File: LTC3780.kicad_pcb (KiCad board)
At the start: 2 copper layers, 120 x 60 mm, 56 parts, among them J1 Screw_Terminal_01x02, J2 Screw_Terminal_01x02, Q2 IPD100N04S402ATMA1, Q3 IPD100N04S402ATMA1, Q4 IPD100N04S402ATMA1, Q5 IPD100N04S402ATMA1, U1 LTC3780EGPBF

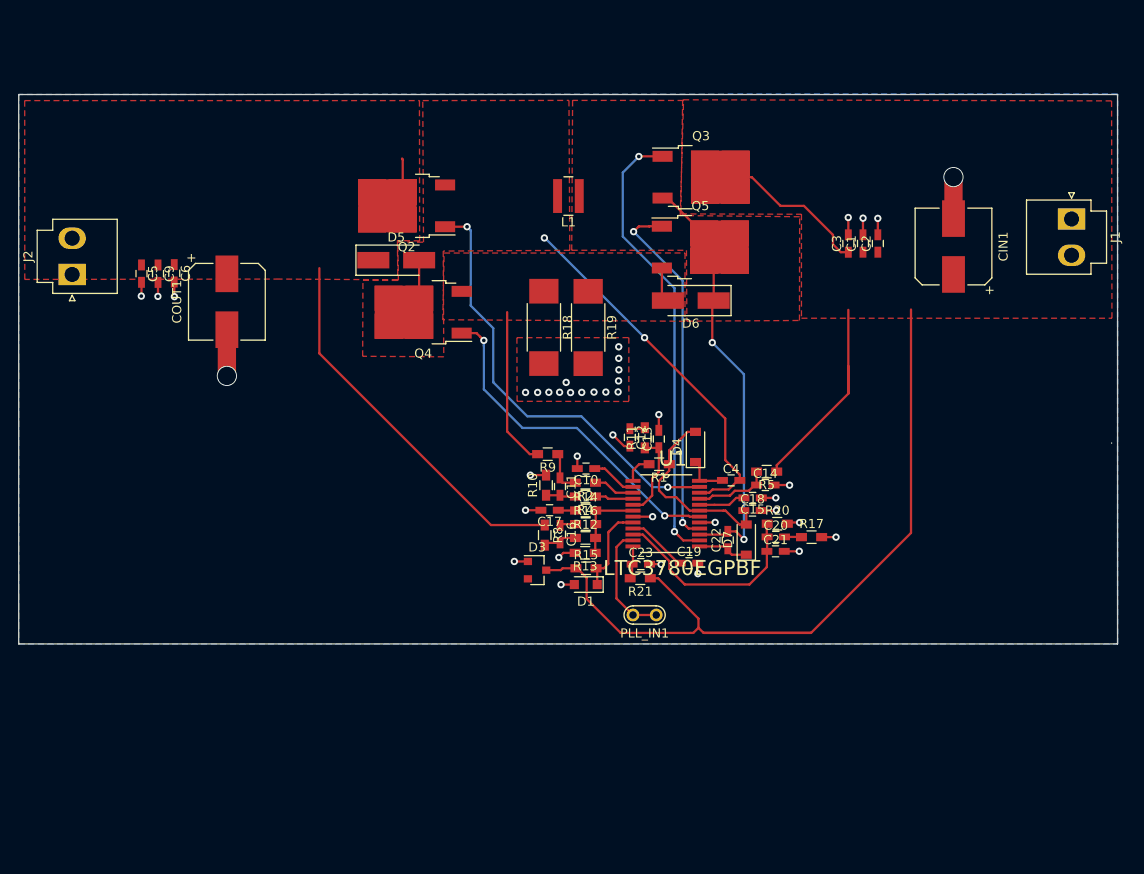
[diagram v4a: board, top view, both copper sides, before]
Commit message: Reduced PCB to 100mm * 60mm and included zip of Gerbers
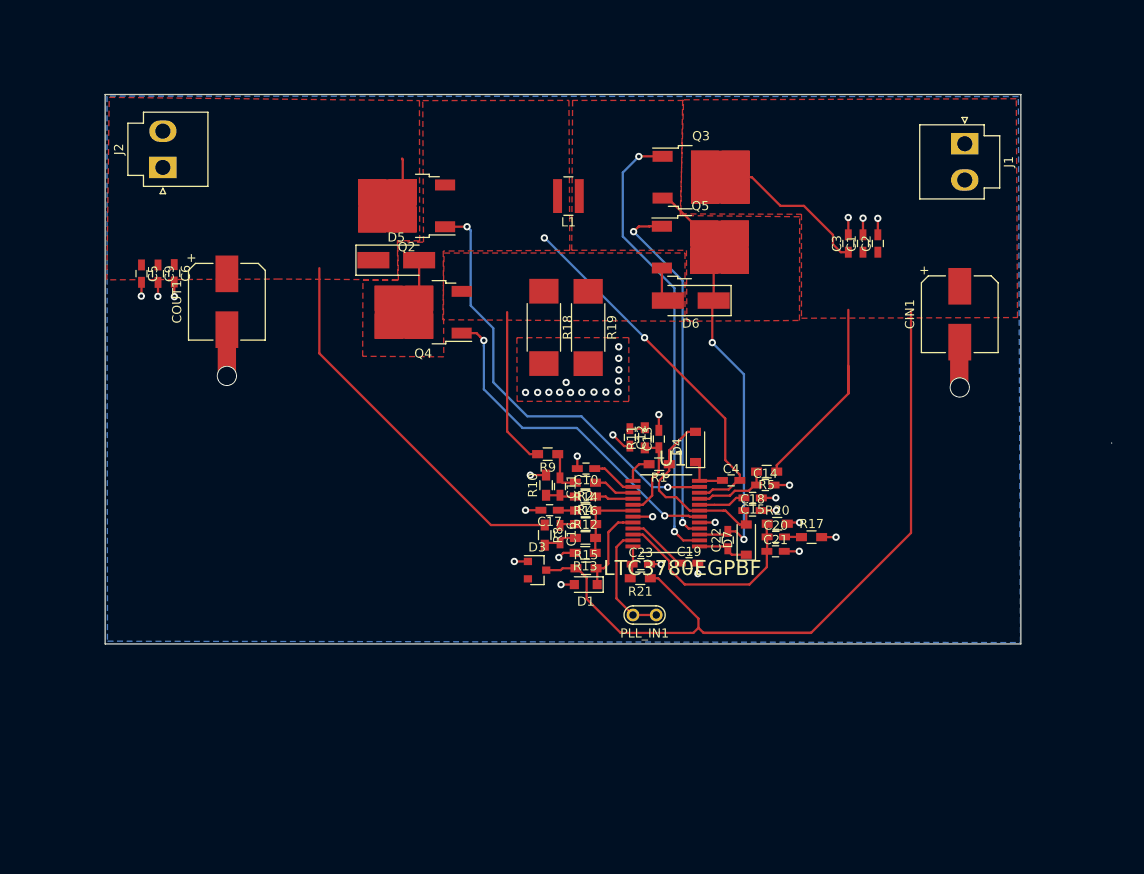
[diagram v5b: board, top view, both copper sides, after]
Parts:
- moved J2 15.3 mm to (124.3, 55.0)
- moved J1 14.3 mm to (211.9, 52.4)
- moved CIN1 7.43 mm to (211.3, 71.0), turned to 270 degrees
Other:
- board size 120 x 60 mm -> 109.9 x 60 mm
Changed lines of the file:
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@@
     (thickness 1.6)
     (drawings 7)
-    (tracks 335)
+    (tracks 334)
     (zones 0)
     (modules 56)
@@
       (outputformat 1)
       (mirror false)
-      (drillshape 1)
+      (drillshape 0)
       (scaleselection 1)
-      (outputdirectory ""))
+      (outputdirectory "/Users/tino/GitHub/LTC3780/gerbers/"))
   )
   (net 0 "")
@@
   )
   (module Connectors_JST:JST_VH_B2P-VH_2x3.96mm_Vertical (layer F.Cu)
-    (at 114.39652 66.66738 90)
+    (at 124.30252 54.9759 90)
     (descr "JST VH series connector, B2P-VH, 3.96mm pitch, top entry type, through hole")
     (tags "connector jst vh vertical")
@@
   )
   (module Connectors_JST:JST_VH_B2P-VH_2x3.96mm_Vertical (layer F.Cu)
-    (at 223.53778 60.60948 270)
+    (at 211.8741 52.39004 270)
     (descr "JST VH series connector, B2P-VH, 3.96mm pitch, top entry type, through hole")
     (tags "connector jst vh vertical")
@@
   )
   (module Capacitors_SMD:CP_Elec_8x6.7 (layer F.Cu)
-    (at 210.6422 63.6143 90)
+    (at 211.328 71.00824 270)
     (descr "SMT capacitor, aluminium electrolytic, 8x6.7")
     (attr smd)
-    (fp_text reference CIN1 (at 0 5.45 90) (layer F.SilkS)
-      (effects (font (size 1 1) (thickness 0.15)))
-    )
-    (fp_text value 22uF (at 0 -5.45 90) (layer F.Fab)
+    (fp_text reference CIN1 (at 0 5.45 270) (layer F.SilkS)
+      (effects (font (size 1 1) (thickness 0.15)))
+    )
+    (fp_text value 22uF (at 0 -5.45 270) (layer F.Fab)
       (effects (font (size 1 1) (thickness 0.15)))
     )
     (fp_circle (center 0 0) (end 1 3.8) (layer F.Fab) (width 0.1))
-    (fp_text user + (at -1.96 -0.08 90) (layer F.Fab)
-      (effects (font (size 1 1) (thickness 0.15)))
-    )
-    (fp_text user + (at -4.78 3.91 90) (layer F.SilkS)
-      (effects (font (size 1 1) (thickness 0.15)))
-    )
-    (fp_text user %R (at 0 5.45 90) (layer F.Fab)
+    (fp_text user + (at -1.96 -0.08 270) (layer F.Fab)
+      (effects (font (size 1 1) (thickness 0.15)))
+    )
+    (fp_text user + (at -4.78 3.91 270) (layer F.SilkS)
+      (effects (font (size 1 1) (thickness 0.15)))
+    )
+    (fp_text user %R (at 0 5.45 270) (layer F.Fab)
       (effects (font (size 1 1) (thickness 0.15)))
     )
@@
     (fp_line (start 5.3 4.29) (end 5.3 -4.29) (layer F.CrtYd) (width 0.05))
     (fp_line (start 5.3 4.29) (end -5.3 4.29) (layer F.CrtYd) (width 0.05))
-    (pad 1 smd rect (at -3.05 0 270) (size 4 2.5) (layers F.Cu F.Paste F.Mask)
+    (pad 1 smd rect (at -3.05 0 90) (size 4 2.5) (layers F.Cu F.Paste F.Mask)
       (net 1 +VSW))
-    (pad 2 smd rect (at 3.05 0 270) (size 4 2.5) (layers F.Cu F.Paste F.Mask)
+    (pad 2 smd rect (at 3.05 0 90) (size 4 2.5) (layers F.Cu F.Paste F.Mask)
       (net 2 GND))
     (model Capacitors_SMD.3dshapes/CP_Elec_8x6.7.wrl
@@
     )
   )
-  (dimension 60.020207 (width 0.15) (layer Dwgs.User)
-    (gr_text "60.00 mm" (at 92 77 90) (layer Dwgs.User)
-      (effects (font (size 1 1) (thickness 0.15)))
-    )
-    (feature1 (pts (xy 108.56468 47.01794) (xy 92.780435 47.010592)))
-    (feature2 (pts (xy 108.53674 107.03814) (xy 92.752495 107.030792)))
-    (crossbar (pts (xy 93.338916 107.031065) (xy 93.366856 47.010865)))
-    (arrow1a (pts (xy 93.366856 47.010865) (xy 93.952752 48.137642)))
-    (arrow1b (pts (xy 93.366856 47.010865) (xy 92.779911 48.137096)))
-    (arrow2a (pts (xy 93.338916 107.031065) (xy 93.925861 105.904834)))
-    (arrow2b (pts (xy 93.338916 107.031065) (xy 92.75302 105.904288)))
-  )
-  (dimension 119.994681 (width 0.15) (layer Dwgs.User)
-    (gr_text "120.00 mm" (at 168.562828 39.37937 360) (layer Dwgs.User)
-      (effects (font (size 1 1) (thickness 0.15)))
-    )
-    (feature1 (pts (xy 228.55936 47.01286) (xy 228.560092 40.099299)))
-    (feature2 (pts (xy 108.56468 47.00016) (xy 108.565412 40.086599)))
-    (crossbar (pts (xy 108.56535 40.67302) (xy 228.56003 40.68572)))
-    (arrow1a (pts (xy 228.56003 40.68572) (xy 227.433464 41.272022)))
-    (arrow1b (pts (xy 228.56003 40.68572) (xy 227.433588 40.09918)))
-    (arrow2a (pts (xy 108.56535 40.67302) (xy 109.691792 41.25956)))
-    (arrow2b (pts (xy 108.56535 40.67302) (xy 109.691916 40.086718)))
+  (dimension 99.979481 (width 0.15) (layer Dwgs.User)
+    (gr_text "100.00 mm" (at 167.995014 42.41734) (layer Dwgs.User)
+      (effects (font (size 1 1) (thickness 0.15)))
+    )
+    (feature1 (pts (xy 118.00586 47.03572) (xy 118.005365 43.137269)))
+    (feature2 (pts (xy 217.98534 47.02302) (xy 217.984845 43.124569)))
+    (crossbar (pts (xy 217.984919 43.71099) (xy 118.005439 43.72369)))
+    (arrow1a (pts (xy 118.005439 43.72369) (xy 119.131868 43.137126)))
+    (arrow1b (pts (xy 118.005439 43.72369) (xy 119.132017 44.309968)))
+    (arrow2a (pts (xy 217.984919 43.71099) (xy 216.858341 43.124712)))
+    (arrow2b (pts (xy 217.984919 43.71099) (xy 216.85849 44.297554)))
+  )
+  (dimension 60.010064 (width 0.15) (layer Dwgs.User)
+    (gr_text "60.00 mm" (at 101.455971 77.023535 89.9) (layer Dwgs.User)
+      (effects (font (size 1 1) (thickness 0.15)))
+    )
+    (feature1 (pts (xy 117.98046 47.03318) (xy 102.196219 47.01915)))
+    (feature2 (pts (xy 117.92712 107.04322) (xy 102.142879 107.02919)))
+    (crossbar (pts (xy 102.7293 107.029711) (xy 102.78264 47.019671)))
+    (arrow1a (pts (xy 102.78264 47.019671) (xy 103.368059 48.146696)))
+    (arrow1b (pts (xy 102.78264 47.019671) (xy 102.195218 48.145653)))
+    (arrow2a (pts (xy 102.7293 107.029711) (xy 103.316722 105.903729)))
+    (arrow2b (pts (xy 102.7293 107.029711) (xy 102.143881 105.902686)))
   )
   (gr_line (start 227.9142 85.09) (end 227.9142 85.0646) (layer Edge.Cuts) (width 0.05))
-  (gr_line (start 108.5596 107.0154) (end 108.5596 47.0154) (layer Edge.Cuts) (width 0.05))
-  (gr_line (start 108.5596 107.0154) (end 228.5596 107.0154) (layer Edge.Cuts) (width 0.05))
-  (gr_line (start 228.5596 47.0154) (end 228.5596 107.0154) (layer Edge.Cuts) (width 0.05))
-  (gr_line (start 108.5596 47.0154) (end 228.5596 47.0154) (layer Edge.Cuts) (width 0.05))
+  (gr_line (start 118 107.0154) (end 118 47.0154) (layer Edge.Cuts) (width 0.05))
+  (gr_line (start 118 107.0154) (end 218 107.0154) (layer Edge.Cuts) (width 0.05))
+  (gr_line (start 218 47.0154) (end 218 107.0154) (layer Edge.Cuts) (width 0.05))
+  (gr_line (start 118 47.0154) (end 218 47.0154) (layer Edge.Cuts) (width 0.05))
   (segment (start 167.75176 98.95586) (end 167.95496 98.75266) (width 0.25) (layer F.Cu) (net 1))
   (segment (start 166.16858 98.95586) (end 167.75176 98.95586) (width 0.25) (layer F.Cu) (net 1) (status 10))
@@
   (segment (start 174.29226 105.80878) (end 181.89448 105.80878) (width 0.25) (layer F.Cu) (net 1))
   (segment (start 199.15886 79.67848) (end 199.15886 76.64482) (width 0.25) (layer F.Cu) (net 1))
-  (segment (start 210.6422 56.03748) (end 210.63712 56.0324) (width 2) (layer F.Cu) (net 2))
-  (via (at 210.63712 56.0324) (size 2.2) (drill 2) (layers F.Cu B.Cu) (net 2))
-  (segment (start 210.6422 60.5643) (end 210.6422 56.03748) (width 2) (layer F.Cu) (net 2) (status 10))
+  (via (at 211.328 79.0067) (size 2.2) (drill 2) (layers F.Cu B.Cu) (net 2))
+  (segment (start 211.27466 79.0829) (end 211.27466 74.55608) (width 2) (layer F.Cu) (net 2) (status 10))
   (via (at 131.2926 77.74432) (size 2.2) (drill 2) (layers F.Cu B.Cu) (net 2))
   (segment (start 131.2926 72.6968) (end 131.2926 77.74432) (width 2) (layer F.Cu) (net 2) (status 10))
@@
     (polygon
       (pts
-        (xy 228.55428 46.9519) (xy 108.55452 47.0154) (xy 108.55706 107.01528) (xy 228.5619 107.0102) (xy 228.55936 46.9519)
+        (xy 217.73134 47.24146) (xy 118.19636 47.18812) (xy 118.2497 106.7181) (xy 217.95486 106.86796) (xy 217.72118 47.23384)
       )
     )
@@
     (polygon
       (pts
-        (xy 227.90912 47.71136) (xy 181.06644 47.59198) (xy 180.86832 60.05322) (xy 194.03822 60.09132) (xy 194.03822 71.44766)
-        (xy 227.94722 71.44766) (xy 227.90658 47.71136)
+        (xy 217.5002 47.47514) (xy 181.06644 47.59198) (xy 180.86832 60.05322) (xy 194.03822 60.09132) (xy 194.03822 71.44766)
+        (xy 217.63228 71.37146)
       )
     )
@@
     (polygon
       (pts
-        (xy 109.21238 47.67834) (xy 152.32126 47.67834) (xy 152.34412 62.99962) (xy 149.91588 62.96914) (xy 149.95652 67.24904)
-        (xy 137.03046 67.16776) (xy 109.22254 67.2084)
+        (xy 118.44274 47.32528) (xy 152.32126 47.67834) (xy 152.34412 62.99962) (xy 149.91588 62.96914) (xy 149.95652 67.24904)
+        (xy 137.03046 67.16776) (xy 118.1862 67.25158)
       )
     )

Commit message: Updated PCB, added routing holes and reordered some components.
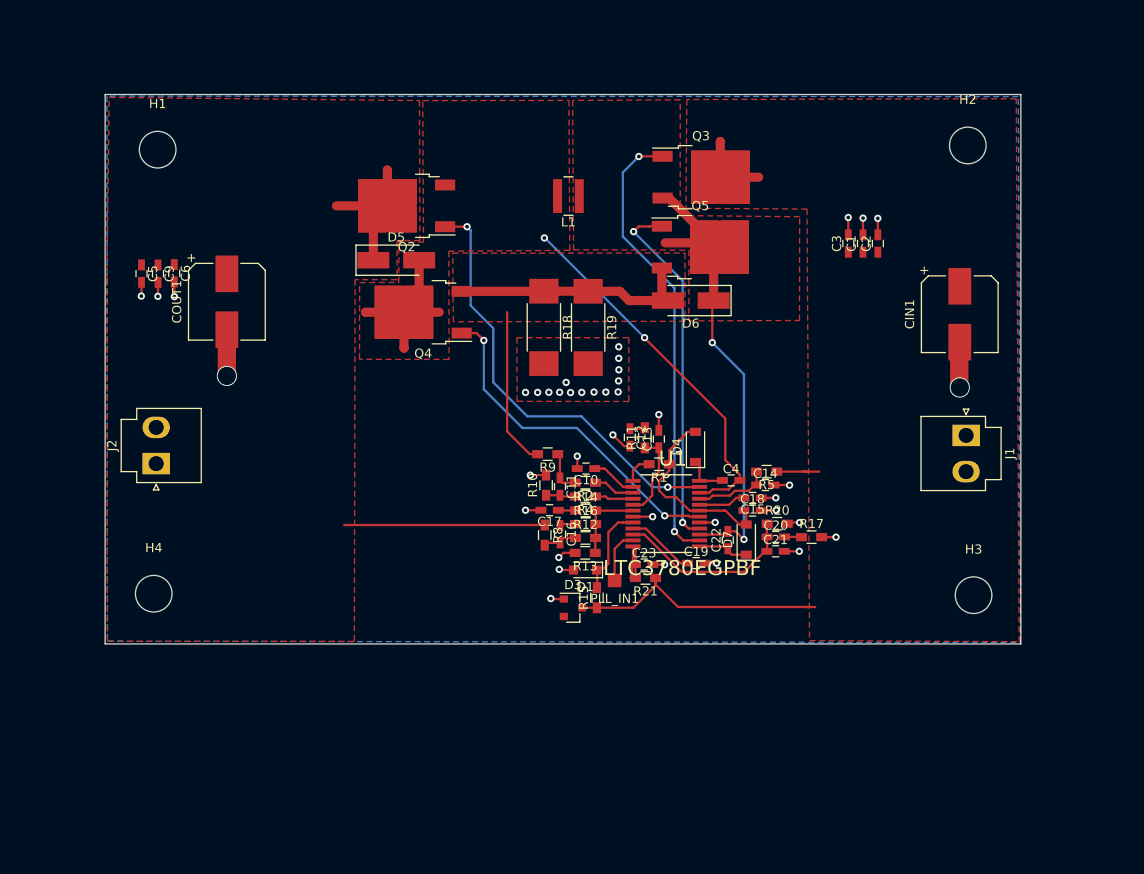
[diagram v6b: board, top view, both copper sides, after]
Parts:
- added H1: MountingHole, Mounting_Holes:MountingHole_4mm, F.Cu at (123.7, 53.0)
- added H2: MountingHole, Mounting_Holes:MountingHole_4mm, F.Cu at (212.2, 52.6)
- added H3: MountingHole, Mounting_Holes:MountingHole_4mm, F.Cu at (212.8, 101.7)
- added H4: MountingHole, Mounting_Holes:MountingHole_4mm, F.Cu at (123.3, 101.5)
- PLL_IN1: footprint Measurement_Points:Test_Point -> Measurement_Points:Measurement_Point_Square-SMD-Pad_Small
- moved J2 32.4 mm to (123.6, 87.3)
- moved J1 31.8 mm to (212.0, 84.2)
- moved PLL_IN1 5.91 mm to (173.6, 100.1)
- moved D3 5.68 mm to (169.1, 103.1)
- moved R15 3.43 mm to (171.7, 102.0), turned to 90 degrees
- moved D1 1.59 mm to (170.4, 98.9)
- moved C19 0.78 mm to (182.5, 98.2)
- moved R21 0.57 mm to (177.0, 99.8)
- moved C23 0.36 mm to (176.9, 98.3)
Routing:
- net +VSW: track 135.3 -> 42.7 mm
- net Net-(D6-Pad2): track 21.2 -> 44.2 mm
- net SW2: track 46.1 -> 63.5 mm
- net SW1: track 46.7 -> 63.4 mm
- net VCC: track 45.4 -> 38.0 mm
- net Net-(PLL_IN1-Pad1): track 12.8 -> 5.82 mm
- net Net-(C23-Pad1): track 3.60 -> 7.15 mm
- net PLLFILTR: track 23.1 -> 20.4 mm
- net Net-(C19-Pad1): track 6.74 -> 7.52 mm
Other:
- board size 109.9 x 60 mm -> 100 x 60 mm
- rule trace_min: 0.2 -> 0.1
- rule via_min_size: 0.4 -> 0.2
